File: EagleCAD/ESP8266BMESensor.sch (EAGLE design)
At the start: 21 parts, among them J1 AMP FCI 10103594-0001LF

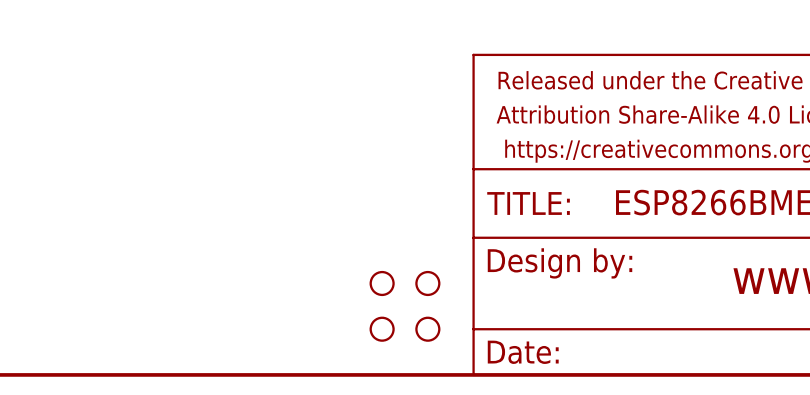
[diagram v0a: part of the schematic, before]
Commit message: updating PCB and adding USB to UART IC
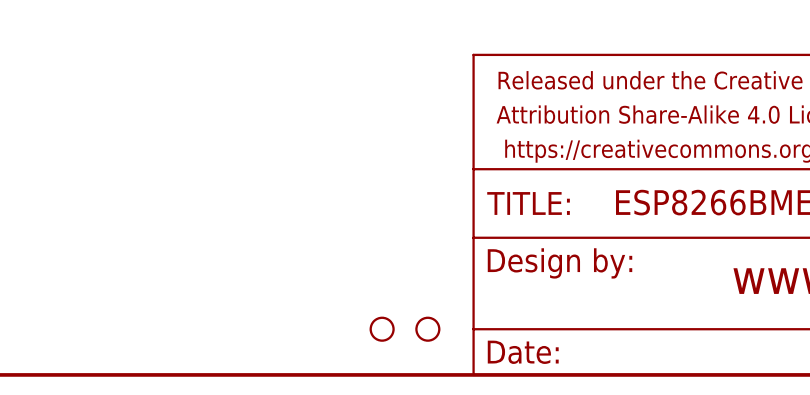
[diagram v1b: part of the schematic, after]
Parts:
- removed H1, H3: STAND-OFF, SparkFun-Hardware:STAND-OFF
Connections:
- net N$4 renamed VCCIO
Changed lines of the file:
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@@
 <setting verticaltext="up"/>
 </settings>
-<grid distance="2.54" unitdist="mm" unit="mm" style="dots" multiple="1" display="no" altdistance="1" altunitdist="mm" altunit="mm"/>
+<grid distance="0.1" unitdist="inch" unit="inch" style="lines" multiple="1" display="no" altdistance="0.01" altunitdist="inch" altunit="inch"/>
 <layers>
 <layer number="1" name="Top" color="4" fill="1" visible="no" active="no"/>
@@
 <part name="JP1" library="adafruit" library_urn="urn:adsk.eagle:library:420" deviceset="PINHD-1X6" device="CB"/>
 <part name="J1" library="SparkFun-Connectors" library_urn="urn:adsk.eagle:library:513" deviceset="USB_MICRO-B" device="_HALF_PTH" package3d_urn="urn:adsk.eagle:package:38241/1" value="AMP FCI 10103594-0001LF"/>
-<part name="H1" library="SparkFun-Hardware" deviceset="STAND-OFF" device=""/>
 <part name="H2" library="SparkFun-Hardware" deviceset="STAND-OFF" device=""/>
-<part name="H3" library="SparkFun-Hardware" deviceset="STAND-OFF" device=""/>
 <part name="H4" library="SparkFun-Hardware" deviceset="STAND-OFF" device=""/>
 <part name="S1" library="SparkFun-Switches" deviceset="MOMENTARY-SWITCH-SPST" device="-PTH-6.0MM"/>
@@
 <instance part="JP1" gate="A" x="86.36" y="172.72" rot="R180"/>
 <instance part="J1" gate="G$1" x="43.18" y="170.18"/>
-<instance part="H1" gate="G$1" x="137.16" y="10.16"/>
 <instance part="H2" gate="G$1" x="137.16" y="5.08"/>
-<instance part="H3" gate="G$1" x="142.24" y="10.16"/>
 <instance part="H4" gate="G$1" x="142.24" y="5.08"/>
 <instance part="S1" gate="G$1" x="43.18" y="119.38"/>
@@
 </segment>
 </net>
-<net name="N$4" class="0">
+<net name="VCCIO" class="0">
 <segment>
 <pinref part="U2" gate="G$1" pin="3V3OUT"/>

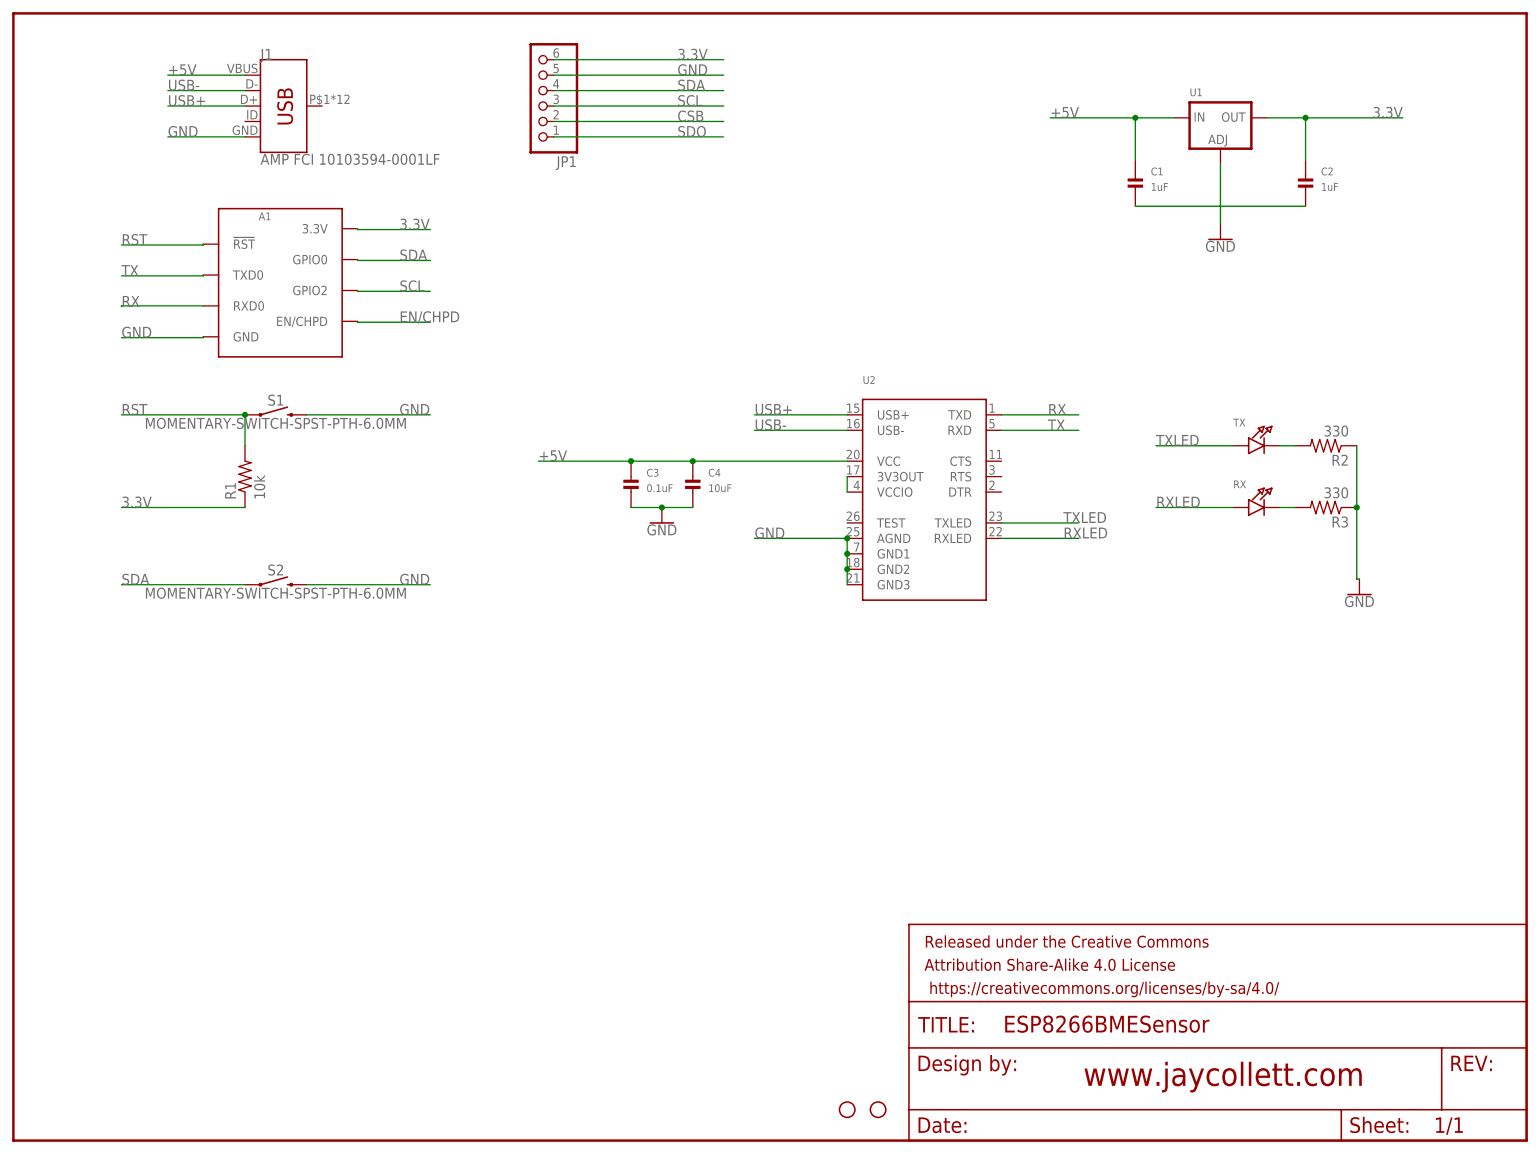
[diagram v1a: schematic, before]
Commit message: fixinng SDA/SCL pins and setting MQTT update to 5 mins
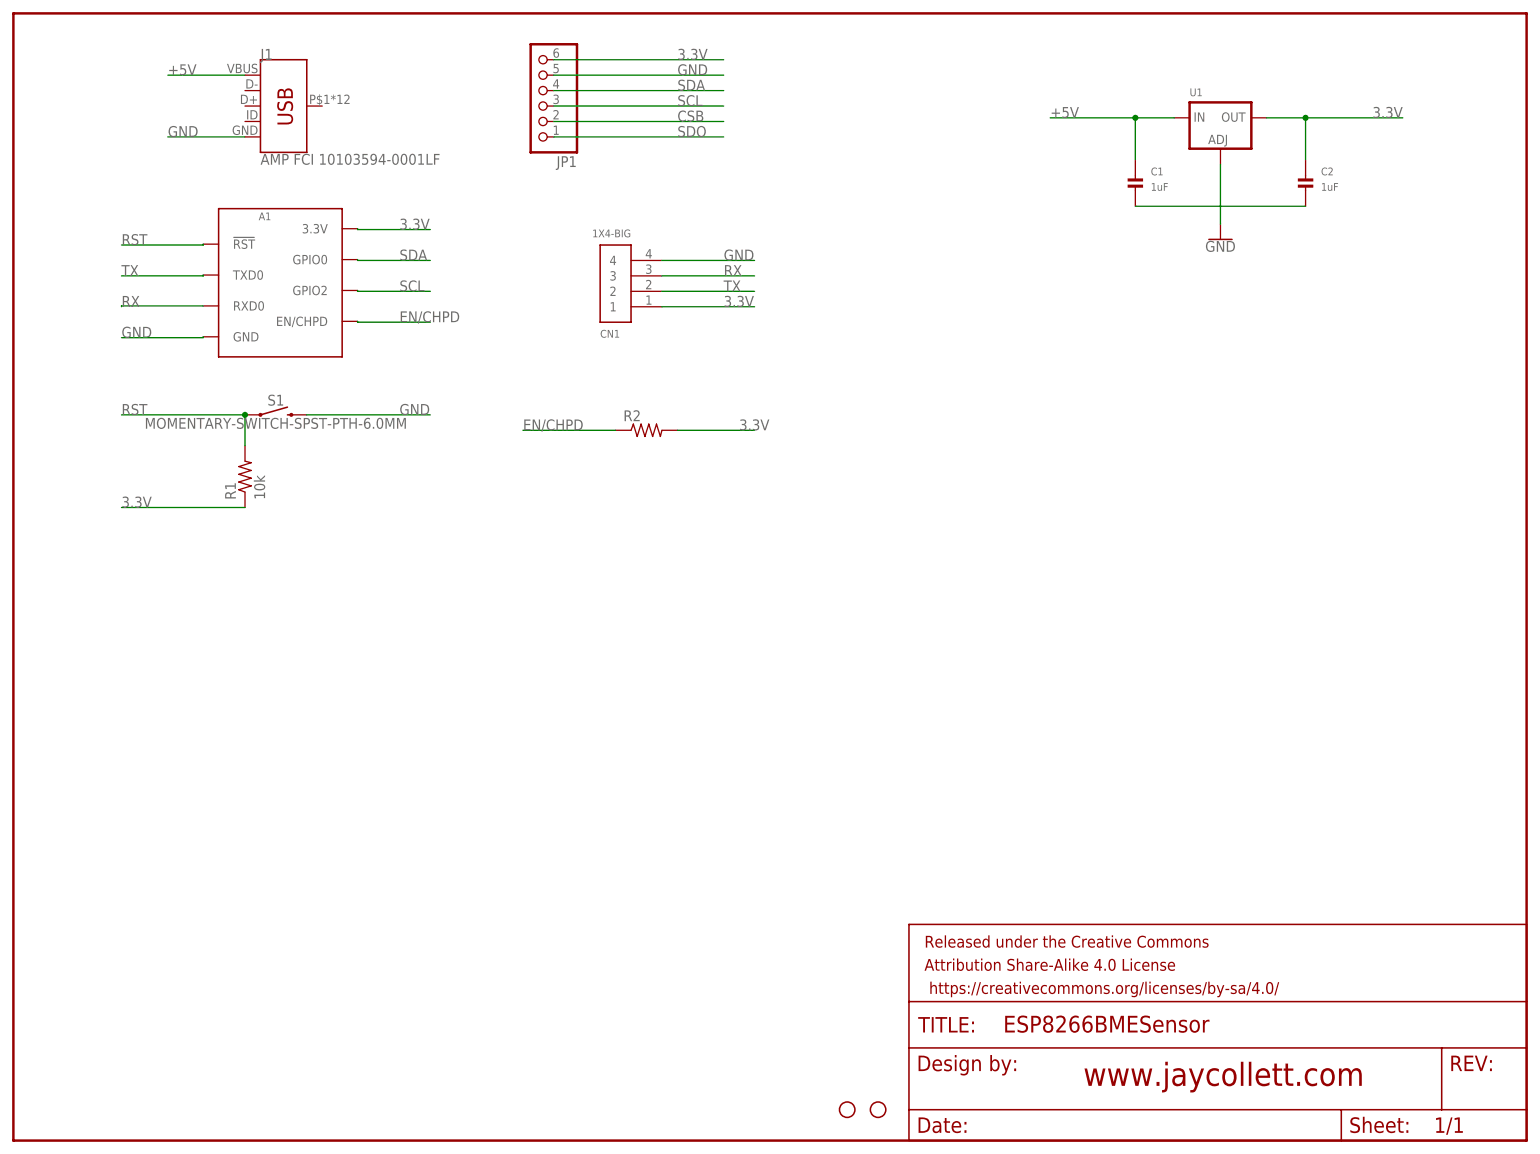
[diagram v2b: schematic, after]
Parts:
- removed C3: 0.1uF, microbuilder:CAP_CERAMIC0805
- removed C4: 10uF, microbuilder:CAP_CERAMIC0805
- removed R3: 330, adafruit:R-US_R0805
- removed RX, TX: (no value), microbuilder:LED0805_NOOUTLINE
- removed S2: MOMENTARY-SWITCH-SPST-PTH-6.0MM, SparkFun-Switches:MOMENTARY-SWITCH-SPST-PTH-6.0MM
- removed U2: (no value), microbuilder:FT232RLSSOP28
- added CN1: 1X4-BIG, adafruit:1X4-BIG
- R2: value 330 -> (none)
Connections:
- removed net N$2: R2.2, TX.C
- removed net N$3: R3.2, RX.C
- removed net RXLED: RX.A, U2.RXLED
- removed net TXLED: TX.A, U2.TXLED
- removed net USB+: J1.D+, U2.USB+
- removed net USB-: J1.D-, U2.USB-
- removed net VCCIO: U2.3V3OUT, U2.VCCIO
- net +5V: no longer C3.P$1, C4.P$1, U2.VCC
- net 3.3V: now also CN1.1, R2.2
- net EN/CHPD: now also R2.1
- net GND: now also CN1.4; no longer C3.P$2, C4.P$2, R2.1, R3.1, S2.2, U2.AGND, U2.GND1, U2.GND2, U2.GND3
- net RX: now also CN1.3; no longer U2.TXD
- net SDA: no longer S2.1
- net TX: now also CN1.2; no longer U2.RXD
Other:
- moved on the sheet: R2
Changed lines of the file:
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@@
 <part name="H4" library="SparkFun-Hardware" deviceset="STAND-OFF" device=""/>
 <part name="S1" library="SparkFun-Switches" deviceset="MOMENTARY-SWITCH-SPST" device="-PTH-6.0MM"/>
-<part name="S2" library="SparkFun-Switches" deviceset="MOMENTARY-SWITCH-SPST" device="-PTH-6.0MM"/>
 <part name="R1" library="adafruit" deviceset="R-US_" device="R0805" value="10k"/>
-<part name="U2" library="microbuilder" deviceset="FT232RL" device="SSOP28"/>
-<part name="TX" library="microbuilder" deviceset="LED" device="0805_NOOUTLINE"/>
-<part name="RX" library="microbuilder" deviceset="LED" device="0805_NOOUTLINE"/>
-<part name="R2" library="adafruit" deviceset="R-US_" device="R0805" value="330"/>
-<part name="R3" library="adafruit" deviceset="R-US_" device="R0805" value="330"/>
-<part name="GND2" library="SparkFun-PowerSymbols" deviceset="GND" device=""/>
-<part name="C3" library="microbuilder" deviceset="CAP_CERAMIC" device="0805" value="0.1uF"/>
-<part name="C4" library="microbuilder" deviceset="CAP_CERAMIC" device="0805" value="10uF"/>
-<part name="GND3" library="SparkFun-PowerSymbols" deviceset="GND" device=""/>
+<part name="CN1" library="adafruit" library_urn="urn:adsk.eagle:library:420" deviceset="1X4" device="-BIG"/>
+<part name="R2" library="adafruit" library_urn="urn:adsk.eagle:library:420" deviceset="R-US_" device="R0805"/>
 </parts>
 <sheets>
@@
 <instance part="H4" gate="G$1" x="142.24" y="5.08"/>
 <instance part="S1" gate="G$1" x="43.18" y="119.38"/>
-<instance part="S2" gate="G$1" x="43.18" y="91.44"/>
 <instance part="R1" gate="G$1" x="38.1" y="109.22" rot="R90"/>
-<instance part="U2" gate="G$1" x="149.86" y="104.14"/>
-<instance part="TX" gate="G$1" x="205.74" y="114.3"/>
-<instance part="RX" gate="G$1" x="205.74" y="104.14"/>
-<instance part="R2" gate="G$1" x="215.9" y="114.3" rot="R180"/>
-<instance part="R3" gate="G$1" x="215.9" y="104.14" rot="R180"/>
-<instance part="GND2" gate="1" x="221.42" y="89.82"/>
-<instance part="C3" gate="G$1" x="101.6" y="106.68"/>
-<instance part="C4" gate="G$1" x="111.76" y="106.68"/>
-<instance part="GND3" gate="1" x="106.68" y="101.6"/>
+<instance part="CN1" gate="G$1" x="101.6" y="139.7" rot="R180"/>
+<instance part="R2" gate="G$1" x="104.14" y="116.84"/>
 </instances>
 <busses>
@@
 </segment>
 <segment>
-<pinref part="S2" gate="G$1" pin="2"/>
-<wire x1="48.26" y1="91.44" x2="68.58" y2="91.44" width="0.1524" layer="91"/>
-<label x="63.5" y="91.44" size="1.778" layer="95"/>
-</segment>
-<segment>
-<pinref part="U2" gate="G$1" pin="AGND"/>
-<pinref part="U2" gate="G$1" pin="GND1"/>
-<wire x1="137.16" y1="99.06" x2="137.16" y2="96.52" width="0.1524" layer="91"/>
-<pinref part="U2" gate="G$1" pin="GND2"/>
-<wire x1="137.16" y1="96.52" x2="137.16" y2="93.98" width="0.1524" layer="91"/>
-<junction x="137.16" y="96.52"/>
-<pinref part="U2" gate="G$1" pin="GND3"/>
-<wire x1="137.16" y1="93.98" x2="137.16" y2="91.44" width="0.1524" layer="91"/>
-<junction x="137.16" y="93.98"/>
-<wire x1="137.16" y1="99.06" x2="121.92" y2="99.06" width="0.1524" layer="91"/>
-<junction x="137.16" y="99.06"/>
-<label x="121.92" y="99.06" size="1.778" layer="95"/>
-</segment>
-<segment>
-<pinref part="R2" gate="G$1" pin="1"/>
-<pinref part="R3" gate="G$1" pin="1"/>
-<wire x1="220.98" y1="114.3" x2="220.98" y2="104.14" width="0.1524" layer="91"/>
-<wire x1="220.98" y1="104.14" x2="220.98" y2="92.36" width="0.1524" layer="91"/>
-<junction x="220.98" y="104.14"/>
-<pinref part="GND2" gate="1" pin="GND"/>
-<wire x1="220.98" y1="92.36" x2="221.42" y2="92.36" width="0.1524" layer="91"/>
-</segment>
-<segment>
-<pinref part="C3" gate="G$1" pin="P$2"/>
-<pinref part="C4" gate="G$1" pin="P$2"/>
-<wire x1="101.6" y1="104.14" x2="106.68" y2="104.14" width="0.1524" layer="91"/>
-<pinref part="GND3" gate="1" pin="GND"/>
-<wire x1="106.68" y1="104.14" x2="111.76" y2="104.14" width="0.1524" layer="91"/>
-<junction x="106.68" y="104.14"/>
+<pinref part="CN1" gate="G$1" pin="4"/>
+<wire x1="106.68" y1="144.78" x2="121.92" y2="144.78" width="0.1524" layer="91"/>
+<label x="116.84" y="144.78" size="1.778" layer="95"/>
 </segment>
 </net>
@@
 <label x="17.78" y="104.14" size="1.778" layer="95"/>
 </segment>
+<segment>
+<pinref part="CN1" gate="G$1" pin="1"/>
+<wire x1="106.68" y1="137.16" x2="121.92" y2="137.16" width="0.1524" layer="91"/>
+<label x="116.84" y="137.16" size="1.778" layer="95"/>
+</segment>
+<segment>
+<pinref part="R2" gate="G$1" pin="2"/>
+<wire x1="109.22" y1="116.84" x2="121.92" y2="116.84" width="0.1524" layer="91"/>
+<label x="119.38" y="116.84" size="1.778" layer="95"/>
+</segment>
 </net>
 <net name="EN/CHPD" class="0">
@@
 <wire x1="56.62" y1="134.62" x2="68.58" y2="134.62" width="0.1524" layer="91"/>
 <label x="63.5" y="134.62" size="1.778" layer="95"/>
+</segment>
+<segment>
+<pinref part="R2" gate="G$1" pin="1"/>
+<wire x1="99.06" y1="116.84" x2="83.82" y2="116.84" width="0.1524" layer="91"/>
+<label x="83.82" y="116.84" size="1.778" layer="95"/>
 </segment>
 </net>
@@
 </segment>
 <segment>
-<pinref part="U2" gate="G$1" pin="RXD"/>
-<wire x1="175.26" y1="116.84" x2="162.56" y2="116.84" width="0.1524" layer="91"/>
-<label x="170.18" y="116.84" size="1.778" layer="95"/>
+<pinref part="CN1" gate="G$1" pin="2"/>
+<wire x1="106.68" y1="139.7" x2="121.92" y2="139.7" width="0.1524" layer="91"/>
+<label x="116.84" y="139.7" size="1.778" layer="95"/>
 </segment>
 </net>
@@
 </segment>
 <segment>
-<pinref part="U2" gate="G$1" pin="TXD"/>
-<wire x1="162.56" y1="119.38" x2="175.26" y2="119.38" width="0.1524" layer="91"/>
-<label x="170.18" y="119.38" size="1.778" layer="95"/>
+<pinref part="CN1" gate="G$1" pin="3"/>
+<wire x1="106.68" y1="142.24" x2="121.92" y2="142.24" width="0.1524" layer="91"/>
+<label x="116.84" y="142.24" size="1.778" layer="95"/>
 </segment>
 </net>
@@
 <label x="63.5" y="144.78" size="1.778" layer="95"/>
 </segment>
-<segment>
-<pinref part="S2" gate="G$1" pin="1"/>
-<wire x1="38.1" y1="91.44" x2="17.78" y2="91.44" width="0.1524" layer="91"/>
-<label x="17.78" y="91.44" size="1.778" layer="95"/>
-</segment>
-</net>
-<net name="USB+" class="0">
-<segment>
-<pinref part="J1" gate="G$1" pin="D+"/>
-<wire x1="38.1" y1="170.18" x2="25.4" y2="170.18" width="0.1524" layer="91"/>
-<label x="25.4" y="170.18" size="1.778" layer="95"/>
-</segment>
-<segment>
-<pinref part="U2" gate="G$1" pin="USB+"/>
-<wire x1="137.16" y1="119.38" x2="121.92" y2="119.38" width="0.1524" layer="91"/>
-<label x="121.92" y="119.38" size="1.778" layer="95"/>
-</segment>
-</net>
-<net name="USB-" class="0">
-<segment>
-<pinref part="J1" gate="G$1" pin="D-"/>
-<wire x1="38.1" y1="172.72" x2="25.4" y2="172.72" width="0.1524" layer="91"/>
-<label x="25.4" y="172.72" size="1.778" layer="95"/>
-</segment>
-<segment>
-<pinref part="U2" gate="G$1" pin="USB-"/>
-<wire x1="137.16" y1="116.84" x2="121.92" y2="116.84" width="0.1524" layer="91"/>
-<label x="121.92" y="116.84" size="1.778" layer="95"/>
-</segment>
-</net>
-<net name="TXLED" class="0">
-<segment>
-<pinref part="U2" gate="G$1" pin="TXLED"/>
-<wire x1="162.56" y1="101.6" x2="175.26" y2="101.6" width="0.1524" layer="91"/>
-<label x="172.72" y="101.6" size="1.778" layer="95"/>
-</segment>
-<segment>
-<pinref part="TX" gate="G$1" pin="A"/>
-<wire x1="200.66" y1="114.3" x2="187.96" y2="114.3" width="0.1524" layer="91"/>
-<label x="187.96" y="114.3" size="1.778" layer="95"/>
-</segment>
-</net>
-<net name="RXLED" class="0">
-<segment>
-<pinref part="U2" gate="G$1" pin="RXLED"/>
-<wire x1="162.56" y1="99.06" x2="175.26" y2="99.06" width="0.1524" layer="91"/>
-<label x="172.72" y="99.06" size="1.778" layer="95"/>
-</segment>
-<segment>
-<pinref part="RX" gate="G$1" pin="A"/>
-<wire x1="200.66" y1="104.14" x2="187.96" y2="104.14" width="0.1524" layer="91"/>
-<label x="187.96" y="104.14" size="1.778" layer="95"/>
-</segment>
-</net>
-<net name="N$2" class="0">
-<segment>
-<pinref part="TX" gate="G$1" pin="C"/>
-<pinref part="R2" gate="G$1" pin="2"/>
-<wire x1="208.28" y1="114.3" x2="210.82" y2="114.3" width="0.1524" layer="91"/>
-</segment>
-</net>
-<net name="N$3" class="0">
-<segment>
-<pinref part="R3" gate="G$1" pin="2"/>
-<pinref part="RX" gate="G$1" pin="C"/>
-<wire x1="210.82" y1="104.14" x2="208.28" y2="104.14" width="0.1524" layer="91"/>
-</segment>
 </net>
 <net name="+5V" class="0">
-<segment>
-<pinref part="C3" gate="G$1" pin="P$1"/>
-<pinref part="C4" gate="G$1" pin="P$1"/>
-<wire x1="101.6" y1="111.76" x2="111.76" y2="111.76" width="0.1524" layer="91"/>
-<wire x1="101.6" y1="111.76" x2="86.36" y2="111.76" width="0.1524" layer="91"/>
-<junction x="101.6" y="111.76"/>
-<label x="86.36" y="111.76" size="1.778" layer="95"/>
-<pinref part="U2" gate="G$1" pin="VCC"/>
-<wire x1="111.76" y1="111.76" x2="137.16" y2="111.76" width="0.1524" layer="91"/>
-<junction x="111.76" y="111.76"/>
-</segment>
 <segment>
 <pinref part="U1" gate="G$1" pin="IN"/>
@@
 </segment>
 </net>
-<net name="VCCIO" class="0">
-<segment>
-<pinref part="U2" gate="G$1" pin="3V3OUT"/>
-<pinref part="U2" gate="G$1" pin="VCCIO"/>
-<wire x1="137.16" y1="109.22" x2="137.16" y2="106.68" width="0.1524" layer="91"/>
-</segment>
-</net>
